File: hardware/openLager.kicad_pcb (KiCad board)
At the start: 4 copper layers, 15.2 x 19 mm, 30 parts, among them J1 CONN_01X06, J2 DM3CS-SF, U1 STM32F411CEUx, U2 SPX3819M5-L-3-3, Y1 CSTCE8M00G15L99

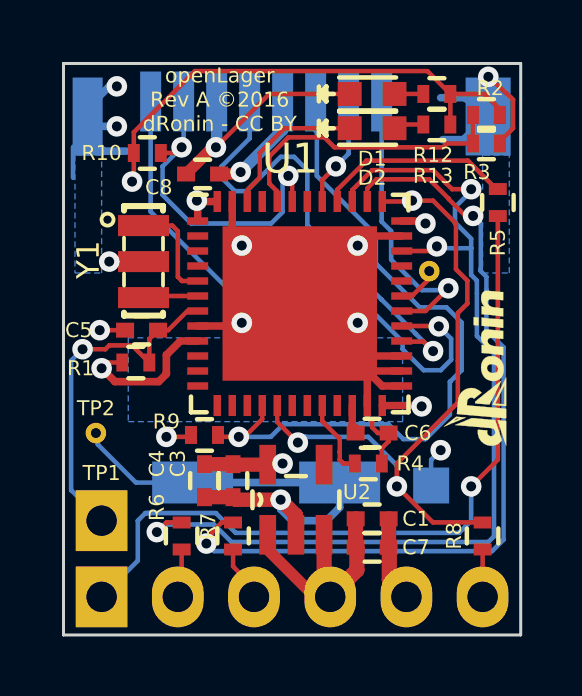
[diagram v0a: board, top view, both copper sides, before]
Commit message: Updated to RevB, changed LED and SS
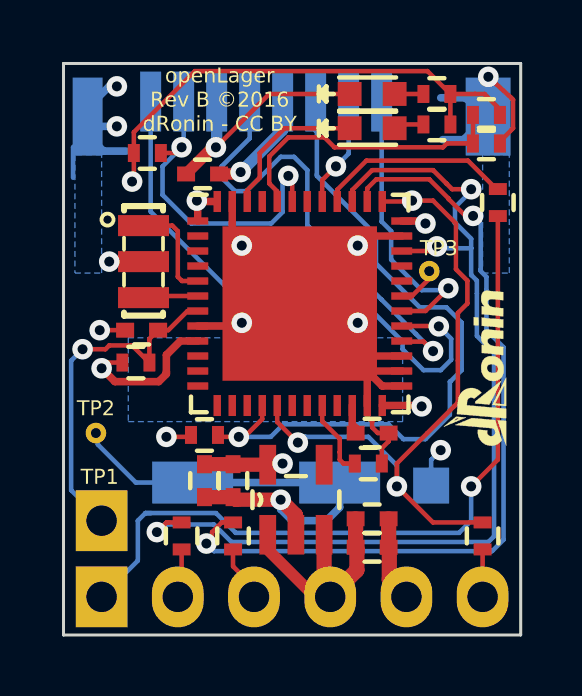
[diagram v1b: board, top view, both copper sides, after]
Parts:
- D1: value APHHS1005CGCK -> LG L29K-F2J1-24
- D2: value APHHS1005SURCK -> LS L29K-G1J2-1-Z
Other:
- board text added: "openLager Rev B ©2016 dRonin - CC BY"
- board text removed: "openLager Rev A ©2016 dRonin - CC BY"
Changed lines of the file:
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@@
     (links 92)
     (no_connects 0)
-    (area 186.709267 94.1961 207.871543 121.981539)
+    (area 186.709267 94.1961 208.776305 121.981539)
     (thickness 1.6)
     (drawings 13)
@@
     (pad_to_paste_clearance_ratio -0.1)
     (aux_axis_origin 0 0)
-    (visible_elements 7FFFFF7F)
+    (visible_elements 7FFFFF5F)
     (pcbplotparams
       (layerselection 0x010fc_80000007)
@@
     (tags "capacitor 0402")
     (attr smd)
-    (fp_text reference C1 (at 1.4605 0) (layer F.SilkS)
+    (fp_text reference C1 (at 1.4605 0) (layer F.SilkS) hide
       (effects (font (size 0.5 0.5) (thickness 0.125)))
     )
@@
     (tags "capacitor 0402")
     (attr smd)
-    (fp_text reference C3 (at -0.5715 1.8415 270) (layer F.SilkS)
+    (fp_text reference C3 (at -0.5715 1.8415 270) (layer F.SilkS) hide
       (effects (font (size 0.5 0.5) (thickness 0.125)))
     )
@@
     (tags "capacitor 0402")
     (attr smd)
-    (fp_text reference C4 (at -0.5715 1.5875 270) (layer F.SilkS)
+    (fp_text reference C4 (at -0.5715 1.5875 270) (layer F.SilkS) hide
       (effects (font (size 0.5 0.5) (thickness 0.125)))
     )
@@
     (tags "capacitor 0402")
     (attr smd)
-    (fp_text reference C5 (at 2.0955 0 180) (layer F.SilkS)
+    (fp_text reference C5 (at 2.0955 0 180) (layer F.SilkS) hide
       (effects (font (size 0.5 0.5) (thickness 0.125)))
     )
@@
     (tags "capacitor 0402")
     (attr smd)
-    (fp_text reference C6 (at 1.524 0) (layer F.SilkS)
+    (fp_text reference C6 (at 1.524 0) (layer F.SilkS) hide
       (effects (font (size 0.5 0.5) (thickness 0.125)))
     )
@@
     (tags "capacitor 0402")
     (attr smd)
-    (fp_text reference C7 (at 1.4605 0) (layer F.SilkS)
+    (fp_text reference C7 (at 1.4605 0) (layer F.SilkS) hide
       (effects (font (size 0.5 0.5) (thickness 0.125)))
     )
@@
     (tags "capacitor 0402")
     (attr smd)
-    (fp_text reference C8 (at 1.4605 -0.4445 180) (layer F.SilkS)
+    (fp_text reference C8 (at 1.4605 -0.4445 180) (layer F.SilkS) hide
       (effects (font (size 0.5 0.5) (thickness 0.125)))
     )
@@
     (solder_mask_margin 0.1)
     (attr smd)
-    (fp_text reference J2 (at 1.524 -13.335) (layer B.SilkS)
+    (fp_text reference J2 (at 1.524 -13.335) (layer B.SilkS) hide
       (effects (font (size 1 1) (thickness 0.15)) (justify mirror))
     )
@@
     (tags "resistor 0402")
     (attr smd)
-    (fp_text reference R1 (at -1.8415 0.1905) (layer F.SilkS)
+    (fp_text reference R1 (at -1.8415 0.1905) (layer F.SilkS) hide
       (effects (font (size 0.5 0.5) (thickness 0.125)))
     )
@@
     (tags "resistor 0402")
     (attr smd)
-    (fp_text reference R2 (at -0.127 0.889 180) (layer F.SilkS)
+    (fp_text reference R2 (at -0.127 0.889 180) (layer F.SilkS) hide
       (effects (font (size 0.5 0.5) (thickness 0.125)))
     )
@@
     (tags "resistor 0402")
     (attr smd)
-    (fp_text reference R3 (at -0.3175 0.9525) (layer F.SilkS)
+    (fp_text reference R3 (at -0.3175 0.9525) (layer F.SilkS) hide
       (effects (font (size 0.5 0.5) (thickness 0.125)))
     )
@@
     (tags "resistor 0402")
     (attr smd)
-    (fp_text reference R4 (at 1.397 0) (layer F.SilkS)
+    (fp_text reference R4 (at 1.397 0) (layer F.SilkS) hide
       (effects (font (size 0.5 0.5) (thickness 0.125)))
     )
@@
     (tags "resistor 0402")
     (attr smd)
-    (fp_text reference R5 (at -1.3335 0 90) (layer F.SilkS)
+    (fp_text reference R5 (at -1.3335 0 90) (layer F.SilkS) hide
       (effects (font (size 0.5 0.5) (thickness 0.125)))
     )
@@
     (tags "resistor 0402")
     (attr smd)
-    (fp_text reference R6 (at 0.9525 -0.8255 90) (layer F.SilkS)
+    (fp_text reference R6 (at 0.9525 -0.8255 90) (layer F.SilkS) hide
       (effects (font (size 0.5 0.5) (thickness 0.125)))
     )
@@
     (tags "resistor 0402")
     (attr smd)
-    (fp_text reference R7 (at 0.3175 -0.8255 90) (layer F.SilkS)
+    (fp_text reference R7 (at 0.3175 -0.8255 90) (layer F.SilkS) hide
       (effects (font (size 0.5 0.5) (thickness 0.125)))
     )
@@
     (tags "resistor 0402")
     (attr smd)
-    (fp_text reference R8 (at 0 -0.9525 90) (layer F.SilkS)
+    (fp_text reference R8 (at 0 -0.9525 90) (layer F.SilkS) hide
       (effects (font (size 0.5 0.5) (thickness 0.125)))
     )
@@
     (tags "resistor 0402")
     (attr smd)
-    (fp_text reference R9 (at -1.27 -0.4445) (layer F.SilkS)
+    (fp_text reference R9 (at -1.27 -0.4445) (layer F.SilkS) hide
       (effects (font (size 0.5 0.5) (thickness 0.125)))
     )
@@
     (tags "resistor 0402")
     (attr smd)
-    (fp_text reference R10 (at -1.524 0) (layer F.SilkS)
+    (fp_text reference R10 (at -1.524 0) (layer F.SilkS) hide
       (effects (font (size 0.5 0.5) (thickness 0.125)))
     )
@@
     (tags "resistor 0402")
     (attr smd)
-    (fp_text reference R12 (at -0.127 2.032) (layer F.SilkS)
+    (fp_text reference R12 (at -0.127 2.032) (layer F.SilkS) hide
       (effects (font (size 0.5 0.5) (thickness 0.125)))
     )
@@
     (tags "resistor 0402")
     (attr smd)
-    (fp_text reference R13 (at 0.127 -1.7145 180) (layer F.SilkS)
+    (fp_text reference R13 (at 0.127 -1.7145 180) (layer F.SilkS) hide
       (effects (font (size 0.5 0.5) (thickness 0.125)))
     )
@@
   (module openLagerFootprints:TP (layer F.Cu)
     (at 202.692 103.4415)
-    (fp_text reference TP3 (at 0 0.5) (layer F.SilkS) hide
-      (effects (font (size 1 1) (thickness 0.15)))
+    (fp_text reference TP3 (at 0.3175 -0.762) (layer F.SilkS)
+      (effects (font (size 0.5 0.5) (thickness 0.125)))
     )
     (fp_text value TEST_1P (at 0 -0.5) (layer F.Fab) hide
@@
     (tags "QFN 0.5")
     (attr smd)
-    (fp_text reference U1 (at -0.3175 -4.826) (layer F.SilkS)
+    (fp_text reference U1 (at -0.3175 -4.826) (layer F.SilkS) hide
       (effects (font (size 1 1) (thickness 0.15)))
     )
@@
     (solder_mask_margin 0.1)
     (attr smd)
-    (fp_text reference Y1 (at -0.0635 1.8415 270) (layer F.SilkS)
+    (fp_text reference Y1 (at -0.0635 1.8415 270) (layer F.SilkS) hide
       (effects (font (size 0.75 0.75) (thickness 0.1)))
     )
@@
     (tags "LED led 0603 SMD smd SMT smt smdled SMDLED smtled SMTLED")
     (attr smd)
-    (fp_text reference D1 (at 0 2.159) (layer F.SilkS)
-      (effects (font (size 0.5 0.5) (thickness 0.125)))
-    )
-    (fp_text value APHHS1005CGCK (at 0 1.5) (layer F.Fab) hide
+    (fp_text reference D1 (at 0 2.159) (layer F.SilkS) hide
+      (effects (font (size 0.5 0.5) (thickness 0.125)))
+    )
+    (fp_text value "LG L29K-F2J1-24" (at 0 1.5) (layer F.Fab) hide
       (effects (font (size 1 1) (thickness 0.15)))
     )
@@
     (tags "LED led 0603 SMD smd SMT smt smdled SMDLED smtled SMTLED")
     (attr smd)
-    (fp_text reference D2 (at 0 1.651) (layer F.SilkS)
-      (effects (font (size 0.5 0.5) (thickness 0.125)))
-    )
-    (fp_text value APHHS1005SURCK (at 0 1.5) (layer F.Fab) hide
+    (fp_text reference D2 (at 0 1.651) (layer F.SilkS) hide
+      (effects (font (size 0.5 0.5) (thickness 0.125)))
+    )
+    (fp_text value "LS L29K-G1J2-1-Z" (at 0 1.5) (layer F.Fab) hide
       (effects (font (size 1 1) (thickness 0.15)))
     )
@@
     (descr "Through hole socket strip")
     (tags "socket strip")
-    (fp_text reference TP1 (at 0 -1.5875) (layer F.SilkS)
+    (fp_text reference TP1 (at -0.0635 -1.4605) (layer F.SilkS)
       (effects (font (size 0.5 0.5) (thickness 0.125)))
     )
@@
     (solder_mask_margin 0.1)
     (attr smd)
-    (fp_text reference U2 (at 0.254 2.032 180) (layer F.SilkS)
+    (fp_text reference U2 (at 0.254 2.032 180) (layer F.SilkS) hide
       (effects (font (size 0.5 0.5) (thickness 0.125)))
     )
@@
     (effects (font (size 0.5 0.5) (thickness 0.1)) (justify mirror))
   )
-  (gr_text "openLager\nRev A ©2016\ndRonin - CC BY" (at 196.85 103.886) (layer B.SilkS)
+  (gr_text "openLager\nRev B ©2016\ndRonin - CC BY" (at 196.85 103.886) (layer B.SilkS)
     (effects (font (size 0.5 0.5) (thickness 0.1)) (justify mirror))
   )
-  (gr_text "openLager\nRev A ©2016\ndRonin - CC BY" (at 195.707 97.7265) (layer F.SilkS)
+  (gr_text "openLager\nRev B ©2016\ndRonin - CC BY" (at 195.707 97.7265) (layer F.SilkS)
     (effects (font (size 0.5 0.5) (thickness 0.1)))
   )
